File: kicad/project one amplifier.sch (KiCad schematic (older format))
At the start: 4 parts

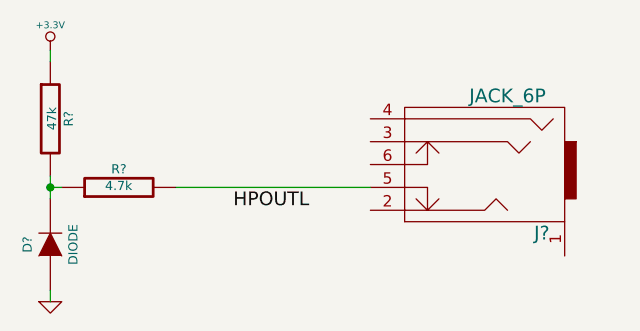
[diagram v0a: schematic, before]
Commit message: Work on amplifier sheeet
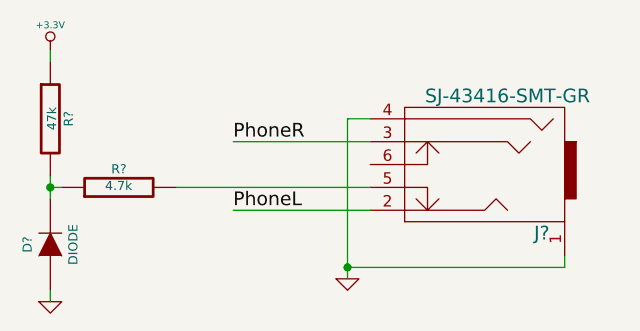
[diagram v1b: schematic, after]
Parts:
- removed J?: JACK_6P, ~, symbol JACK_6P
- added J?: SJ-43416-SMT-GR, ~, symbol JACK_6P
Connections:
- net GND: now also J?.1, J?.4
- net at R?.2: now also J?.5
- new net PhoneL: J?.2
- new net PhoneR: J?.3
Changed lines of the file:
@@
 $EndDescr
-$Comp
-L JACK_6P J?
-U 1 1 5367415C
-P 9350 4900
-F 0 "J?" H 9050 4650 60  0000 C CNN
-F 1 "JACK_6P" H 9200 5250 60  0000 C CNN
-F 2 "~" H 9350 4900 60  0000 C CNN
-F 3 "~" H 9350 4900 60  0000 C CNN
-	1    9350 4900
-	-1   0    0    -1
-$EndComp
 $Comp
 L R R?
@@
 	7500 5450 7500 5400
 Wire Wire Line
-	7500 5000 7500 4950
-Wire Wire Line
-	7500 4950 7500 4900
+	7500 4900 7500 5000
 Wire Wire Line
 	7500 4950 7550 4950
@@
 	7500 4350 7500 4400
 Text Label 8300 5050 0    60   ~ 0
-HPOUTL
+PhoneL
+Wire Wire Line
+	8300 5050 8900 5050
+Text Label 8300 4750 0    60   ~ 0
+PhoneR
+Wire Wire Line
+	8300 4750 8900 4750
+$Comp
+L GND #PWR?
+U 1 1 5367F839
+P 8800 5350
+F 0 "#PWR?" H 8800 5350 30  0001 C CNN
+F 1 "GND" H 8800 5280 30  0001 C CNN
+F 2 "" H 8800 5350 60  0000 C CNN
+F 3 "" H 8800 5350 60  0000 C CNN
+	1    8800 5350
+	1    0    0    -1
+$EndComp
+Wire Wire Line
+	8800 5350 8800 4650
+Wire Wire Line
+	8800 4650 8900 4650
+Wire Wire Line
+	9750 5250 9750 5300
+Wire Wire Line
+	9750 5300 8800 5300
+Connection ~ 8800 5300
+$Comp
+L JACK_6P J?
+U 1 1 5367FDDB
+P 9350 4900
+F 0 "J?" H 9050 4650 60  0000 C CNN
+F 1 "SJ-43416-SMT-GR" H 9200 5250 60  0000 C CNN
+F 2 "~" H 9350 4900 60  0000 C CNN
+F 3 "~" H 9350 4900 60  0000 C CNN
+	1    9350 4900
+	-1   0    0    -1
+$EndComp
 $EndSCHEMATC

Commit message: Version 0.0.0
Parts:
- added C? (x2): 100nF, ~, symbol CSMALL
- added C?: 470uF, ~, symbol CPSMALL
- added C? (x7): 1uF, ~, symbol CSMALL
- added C? (x2): 220pF, ~, symbol C
- added C? (x4): 0.22uF, ~, symbol CSMALL
- added C? (x4): C_FILT, ~, symbol CSMALL
- added L? (x4): L_FILT, ~, symbol INDUCTOR_SMALL
- added R? (x5): 10k, ~, symbol R
- added R? (x2): 5.6k, ~, symbol R
- added R? (x2): R, ~, symbol R
- added SP?: SPK_R, ~, symbol SPEAKER
- added SP?: SPK_L, ~, symbol SPEAKER
- added U?: TAS5760MD, ~, symbol TAS5760MD
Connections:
- net labels added: +12V, DR_MUTE, HP_DETECT, HP_IN L, HP_IN R, HP_OUT L, HP_OUT R, IISC, IISC_IMCK, IISC_ISCK, IISC_ISDO, IISC_IWS, SPK_FAULT, SPK_SD, TWIMS0, TWIMS0_TWCK, TWIMS0_TWD
- net labels removed: PhoneL, PhoneR
- wire segments 11 -> 161
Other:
- note added: "Is SPK_OUTA left, or is SPK_OUTB?"
- note added: "What UVE ratio is needed?"
- note added: "What are the values for\nthe filter components?"
- moved on the sheet: D?, J?, R?

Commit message: Forgot to add annotation
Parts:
- gave numbers to parts that had none: 40

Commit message: Begin switch to analog power amp
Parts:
- removed C601, C602: 220pF, ~, symbol C
- removed C603, C604, C605, C606, C607, C608, C614: 1uF, ~, symbol CSMALL
- removed C609: 470uF, ~, symbol CPSMALL
- removed C610, C611: 100nF, ~, symbol CSMALL
- removed C612, C613, C615, C616: 0.22uF, ~, symbol CSMALL
- removed C617, C618, C619, C620: C_FILT, ~, symbol CSMALL
- removed L601, L602, L603, L604: L_FILT, ~, symbol INDUCTOR_SMALL
- removed R601, R602, R604, R605, R607: 10k, ~, symbol R
- removed R603, R606: 5.6k, ~, symbol R
- removed R608, R610: R, ~, symbol R
- removed SP601: SPK_L, ~, symbol SPEAKER
- removed SP602: SPK_R, ~, symbol SPEAKER
- removed U601: TAS5760MD, ~, symbol TAS5760MD
- added C?: 1uF, ~, symbol CSMALL
- added U?: TPA3116D2, symbol TPA3116D2
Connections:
- net labels removed: +12V, DR_MUTE, HP_IN L, HP_IN R, IISC, IISC_IMCK, IISC_ISCK, IISC_ISDO, IISC_IWS, SPK_FAULT, SPK_SD, TWIMS0, TWIMS0_TWCK, TWIMS0_TWD
- wire segments 161 -> 24
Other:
- note removed: "Is SPK_OUTA left, or is SPK_OUTB?"
- note removed: "What UVE ratio is needed?"
- note removed: "What are the values for\nthe filter components?"
